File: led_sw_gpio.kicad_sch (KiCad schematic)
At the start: 33 parts, among them Q4 2N7002, SW1 up, SW2 down, SW3 left, SW4 rigth, SW5 up, SW6 down

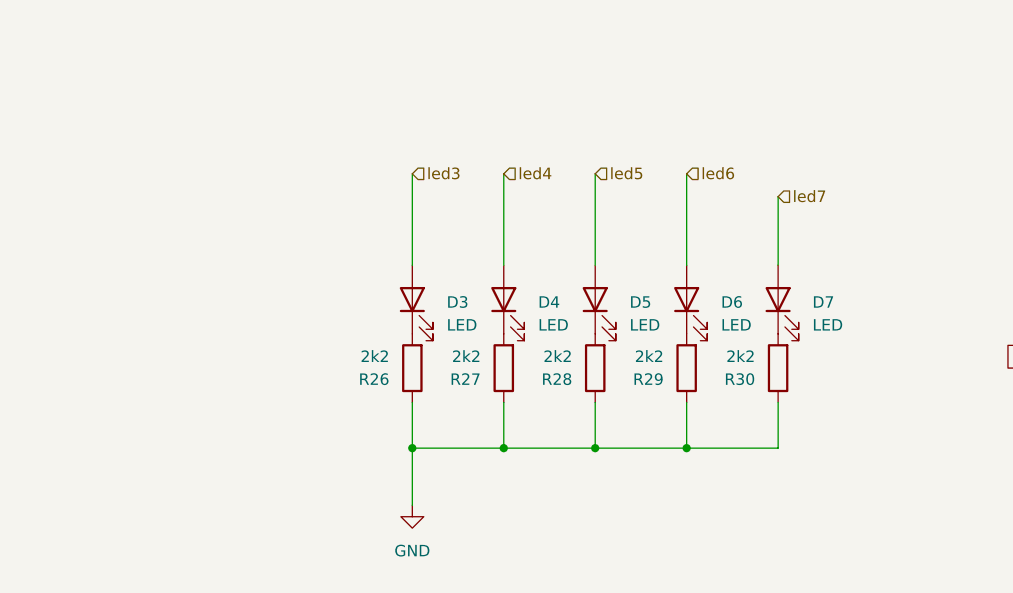
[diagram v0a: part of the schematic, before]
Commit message: se agrego osciloscoio
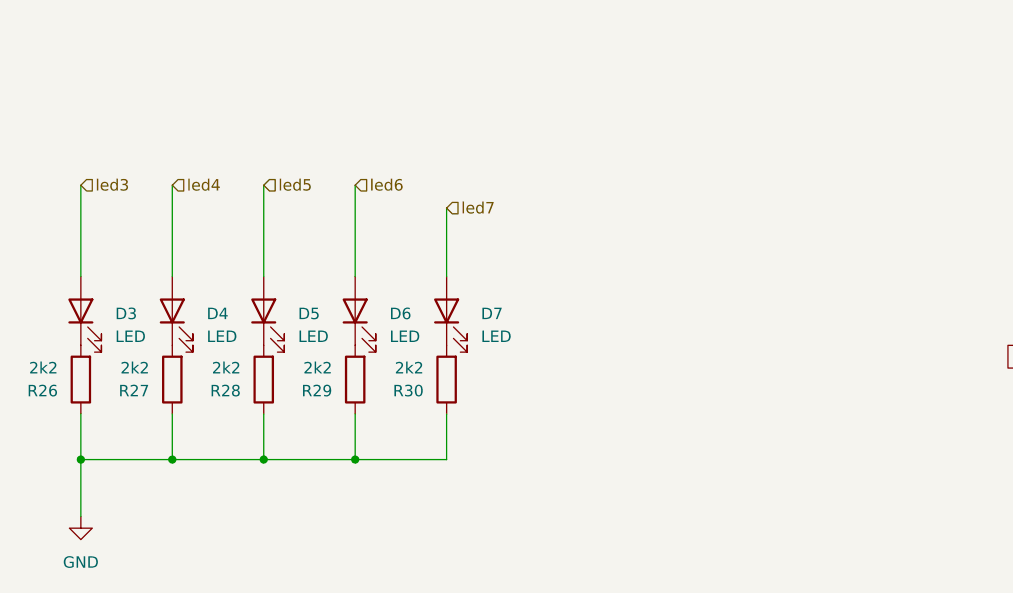
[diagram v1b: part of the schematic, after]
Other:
- moved on the sheet: D3, D4, D5, D6, D7, R26, R27, R28, R29, R30
